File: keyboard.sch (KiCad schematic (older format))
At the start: 30 parts, among them IC1 ATMEGA32U4, J1 USB C, X1 ASX3F

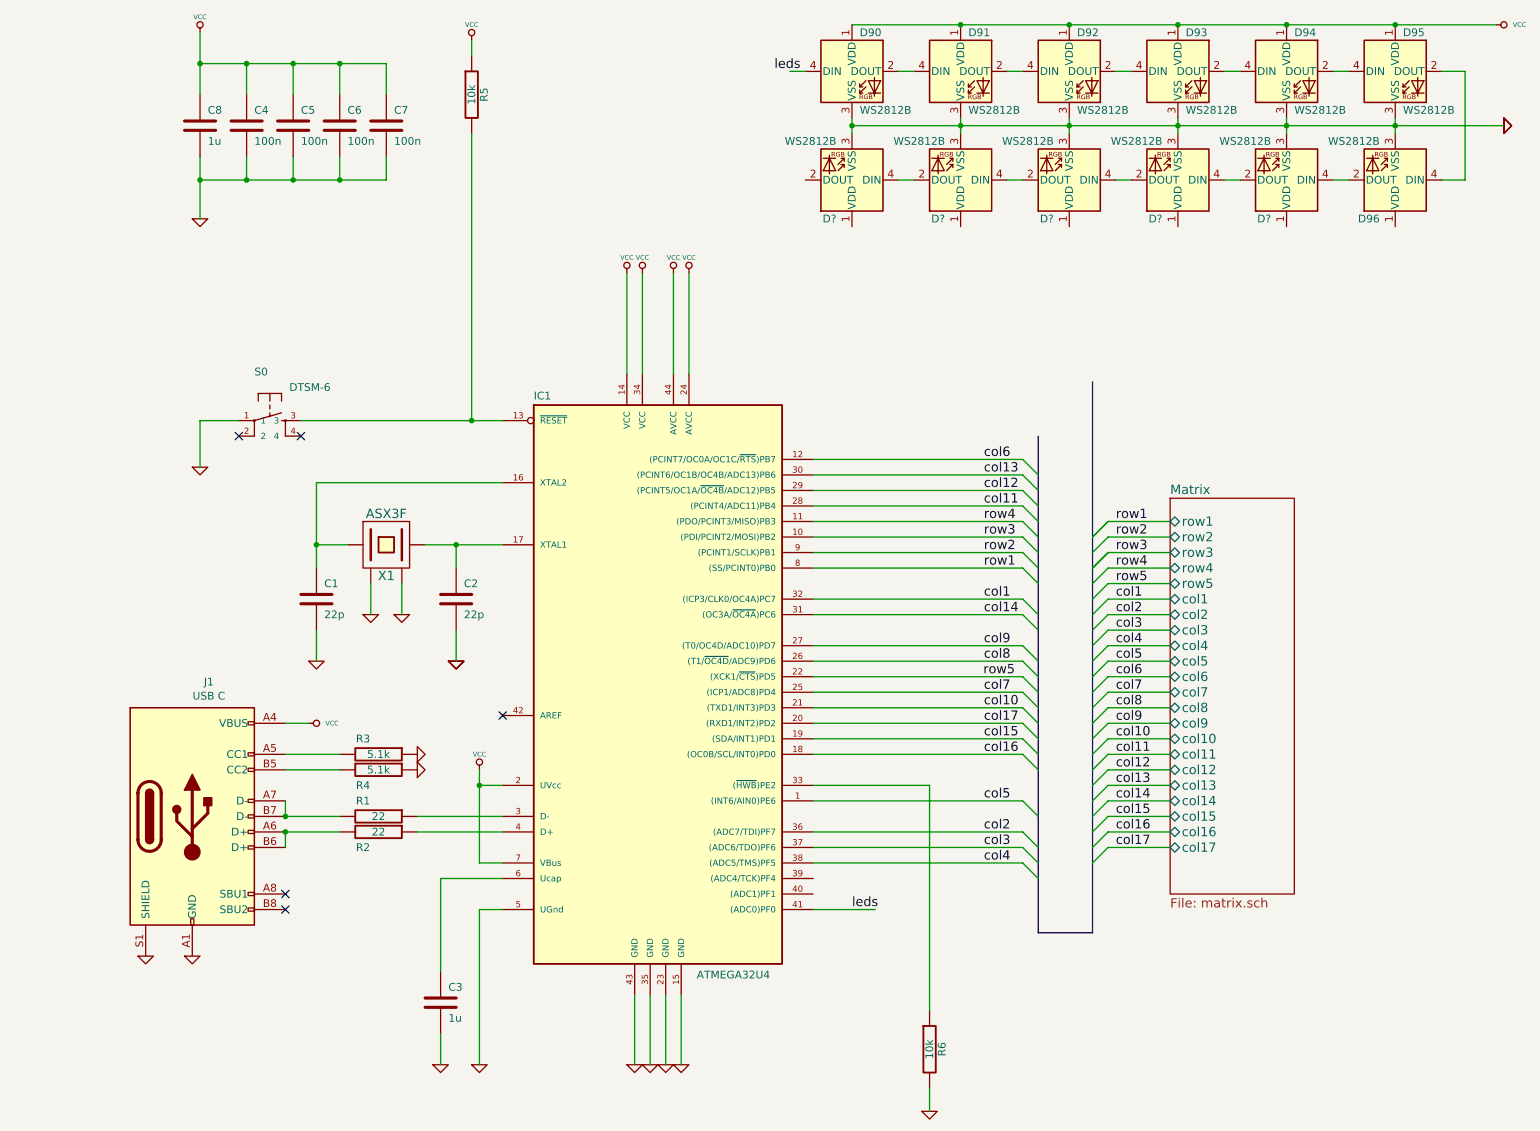
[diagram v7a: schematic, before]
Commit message: Add VCC to all leds
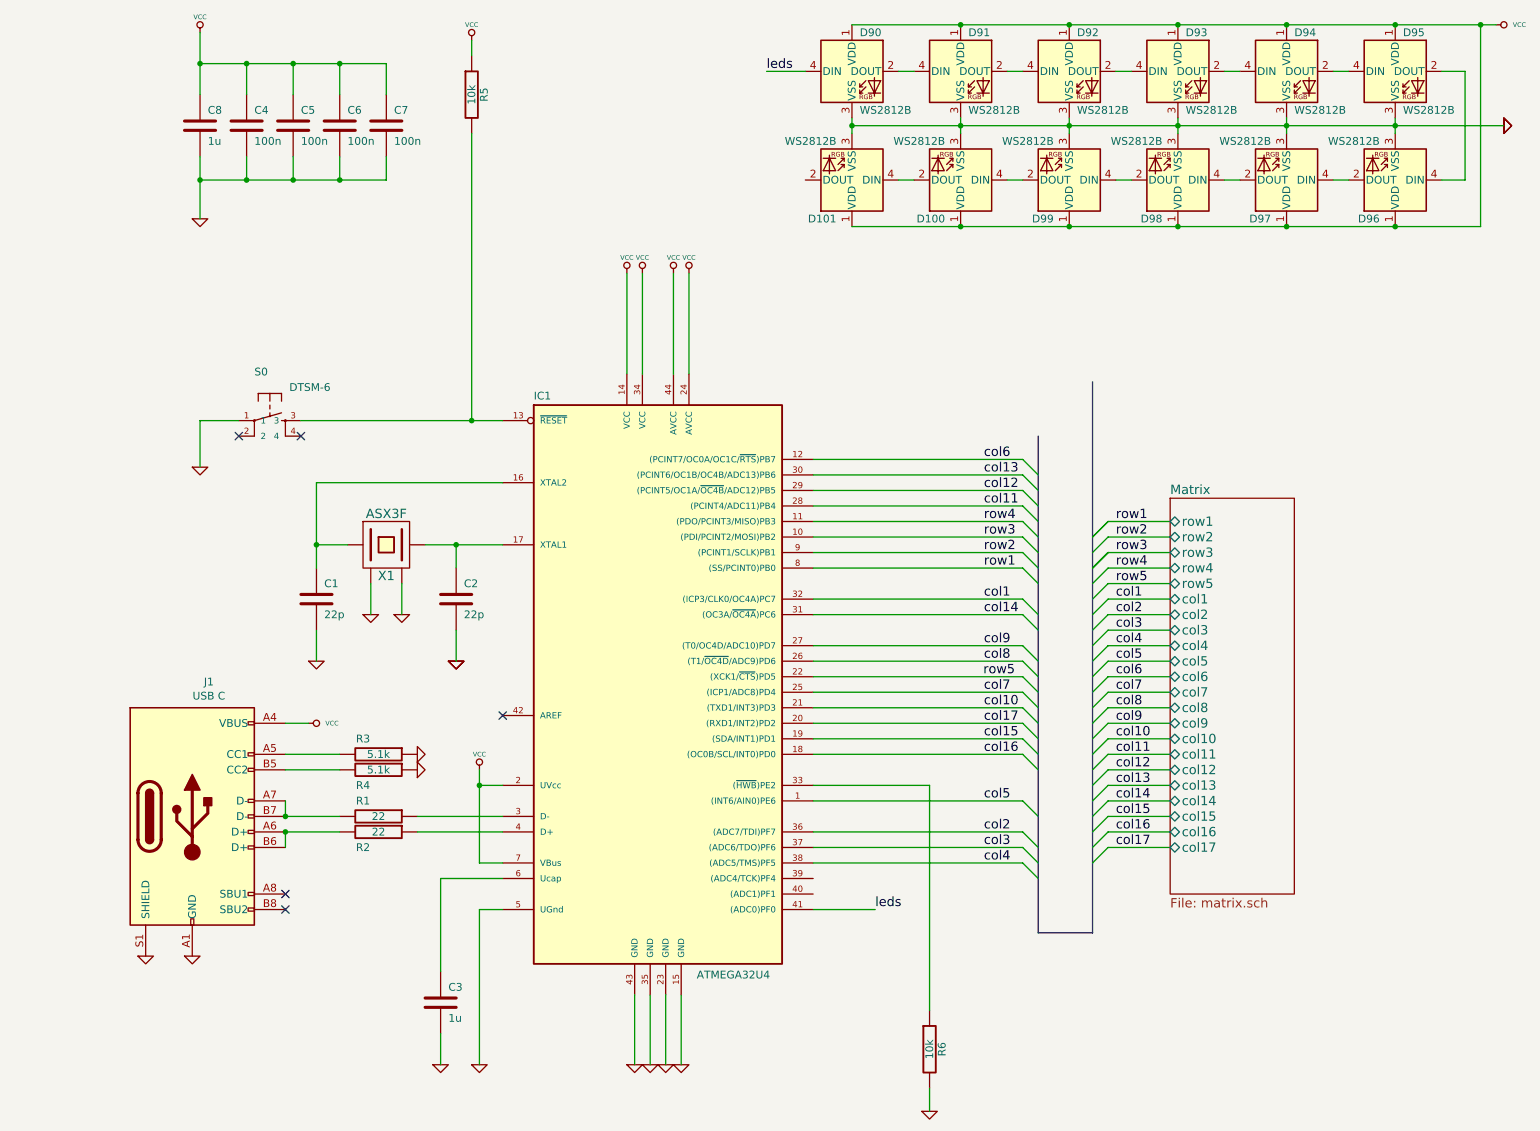
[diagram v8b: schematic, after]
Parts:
- gave numbers to parts that had none: 5
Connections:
- net VCC: now also D100.1 (VDD), D101.1 (VDD), D96.1 (VDD), D97.1 (VDD), D98.1 (VDD), D99.1 (VDD)
- net leds: now also D90.4 (DIN)
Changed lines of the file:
@@
 NoConn ~ 2450 6350
-$Comp
-L LED:WS2812B D90
-U 1 1 61EB4974
-P 6100 950
-F 0 "D90" H 6150 1200 50  0000 L CNN
-F 1 "WS2812B" H 6150 700 50  0000 L CNN
-F 2 "LED_SMD:LED_WS2812B_PLCC4_5.0x5.0mm_P3.2mm" H 6150 650 50  0001 L TNN
-F 3 "https://cdn-shop.adafruit.com/datasheets/WS2812B.pdf" H 6200 575 50  0001 L TNN
-	1    6100 950
-	1    0    0    -1
-$EndComp
 $Comp
 L LED:WS2812B D91
@@
 $EndComp
 $Comp
-L LED:WS2812B D?
+L LED:WS2812B D97
 U 1 1 61EF4C2A
 P 8900 1650
-F 0 "D?" H 9000 1900 50  0000 L CNN
+F 0 "D97" H 9000 1900 50  0000 L CNN
 F 1 "WS2812B" H 9000 1400 50  0000 L CNN
 F 2 "LED_SMD:LED_WS2812B_PLCC4_5.0x5.0mm_P3.2mm" H 8950 1350 50  0001 L TNN
@@
 $EndComp
 $Comp
-L LED:WS2812B D?
+L LED:WS2812B D98
 U 1 1 61EF94FC
 P 8200 1650
-F 0 "D?" H 8300 1900 50  0000 L CNN
+F 0 "D98" H 8300 1900 50  0000 L CNN
 F 1 "WS2812B" H 8300 1400 50  0000 L CNN
 F 2 "LED_SMD:LED_WS2812B_PLCC4_5.0x5.0mm_P3.2mm" H 8250 1350 50  0001 L TNN
@@
 $EndComp
 $Comp
-L LED:WS2812B D?
+L LED:WS2812B D99
 U 1 1 61EFDB1D
 P 7500 1650
-F 0 "D?" H 7600 1900 50  0000 L CNN
+F 0 "D99" H 7600 1900 50  0000 L CNN
 F 1 "WS2812B" H 7600 1400 50  0000 L CNN
 F 2 "LED_SMD:LED_WS2812B_PLCC4_5.0x5.0mm_P3.2mm" H 7550 1350 50  0001 L TNN
@@
 $EndComp
 $Comp
-L LED:WS2812B D?
+L LED:WS2812B D100
 U 1 1 61F02268
 P 6800 1650
-F 0 "D?" H 6900 1900 50  0000 L CNN
+F 0 "D100" H 6900 1900 50  0000 L CNN
 F 1 "WS2812B" H 6900 1400 50  0000 L CNN
 F 2 "LED_SMD:LED_WS2812B_PLCC4_5.0x5.0mm_P3.2mm" H 6850 1350 50  0001 L TNN
@@
 $EndComp
 $Comp
-L LED:WS2812B D?
+L LED:WS2812B D101
 U 1 1 61F069B3
 P 6100 1650
-F 0 "D?" H 6200 1900 50  0000 L CNN
+F 0 "D101" H 6200 1900 50  0000 L CNN
 F 1 "WS2812B" H 6200 1400 50  0000 L CNN
 F 2 "LED_SMD:LED_WS2812B_PLCC4_5.0x5.0mm_P3.2mm" H 6150 1350 50  0001 L TNN
@@
 $EndComp
 Wire Wire Line
-	5700 950  5800 950
-Wire Wire Line
 	6400 950  6500 950
 Wire Wire Line
@@
 Wire Wire Line
 	6500 1650 6400 1650
-Text Label 5600 950  0    60   ~ 0
+Text Label 5550 950  0    60   ~ 0
 leds
 Wire Wire Line
 	5850 6350 6250 6350
-Text Label 6100 6350 0    60   ~ 0
+Text Label 6250 6350 0    60   ~ 0
 leds
 Wire Wire Line
@@
 Connection ~ 8900 650
 Wire Wire Line
-	9600 650  10250 650
+	9600 650  10150 650
 Connection ~ 9600 650
 $Comp
@@
 Wire Wire Line
 	9600 1250 9600 1300
+Wire Wire Line
+	6100 1950 6800 1950
+Wire Wire Line
+	6800 1950 7500 1950
+Connection ~ 6800 1950
+Wire Wire Line
+	7500 1950 8200 1950
+Connection ~ 7500 1950
+Wire Wire Line
+	8200 1950 8900 1950
+Connection ~ 8200 1950
+Wire Wire Line
+	8900 1950 9600 1950
+Connection ~ 8900 1950
+Wire Wire Line
+	9600 1950 10150 1950
+Wire Wire Line
+	10150 1950 10150 650
+Connection ~ 9600 1950
+Connection ~ 10150 650
+Wire Wire Line
+	10150 650  10250 650
+$Comp
+L LED:WS2812B D90
+U 1 1 61EB4974
+P 6100 950
+F 0 "D90" H 6150 1200 50  0000 L CNN
+F 1 "WS2812B" H 6150 700 50  0000 L CNN
+F 2 "LED_SMD:LED_WS2812B_PLCC4_5.0x5.0mm_P3.2mm" H 6150 650 50  0001 L TNN
+F 3 "https://cdn-shop.adafruit.com/datasheets/WS2812B.pdf" H 6200 575 50  0001 L TNN
+	1    6100 950
+	1    0    0    -1
+$EndComp
+Wire Wire Line
+	5800 950  5550 950
 Wire Bus Line
 	7300 3300 7300 6500
